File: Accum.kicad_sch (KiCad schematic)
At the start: 0 parts

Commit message: VER1.0: добавил схему в пдф
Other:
- note added: "Аналоговый сигнал"
- note added: "Арматура накопителя"
- note added: "Питание 24В"
- note added: "Управление 24В"
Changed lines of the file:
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@@
+	)
+	(rectangle
+		(start 146.05 88.9)
+		(end 490.22 325.12)
+		(stroke
+			(width 0.762)
+			(type dash)
+			(color 0 0 0 1)
+		)
+		(fill
+			(type none)
+		)
 	)
 	(rectangle
@@
 		)
 	)
+	(text "Питание 24В"
+		(exclude_from_sim no)
+		(at 73.66 361.95 0)
+		(effects
+			(font
+				(face "Calibri")
+				(size 2.54 2.54)
+				(thickness 0.254)
+				(bold yes)
+				(italic yes)
+				(color 0 0 0 1)
+			)
+			(justify left)
+		)
+	)
+	(text "Аналоговый сигнал"
+		(exclude_from_sim no)
+		(at 73.66 351.79 0)
+		(effects
+			(font
+				(face "Calibri")
+				(size 2.54 2.54)
+				(thickness 0.254)
+				(bold yes)
+				(italic yes)
+				(color 0 0 0 1)
+			)
+			(justify left)
+		)
+	)
 	(text "Р"
 		(exclude_from_sim no)
@@
 		)
 	)
+	(text "Управление 24В"
+		(exclude_from_sim no)
+		(at 73.66 367.03 0)
+		(effects
+			(font
+				(face "Calibri")
+				(size 2.54 2.54)
+				(thickness 0.254)
+				(bold yes)
+				(italic yes)
+				(color 0 0 0 1)
+			)
+			(justify left)
+		)
+	)
+	(text "Арматура накопителя"
+		(exclude_from_sim no)
+		(at 313.944 109.22 0)
+		(effects
+			(font
+				(face "Calibri")
+				(size 6.35 6.35)
+				(italic yes)
+				(color 0 0 0 1)
+			)
+		)
+	)
 	(text "+24В"
 		(exclude_from_sim no)
@@
 				(color 0 0 0 1)
 			)
+		)
+	)
+	(text "CAN сеть"
+		(exclude_from_sim no)
+		(at 73.66 356.87 0)
+		(effects
+			(font
+				(face "Calibri")
+				(size 2.54 2.54)
+				(thickness 0.254)
+				(bold yes)
+				(italic yes)
+				(color 0 0 0 1)
+			)
+			(justify left)
 		)
 	)
@@
 			(width 0.762)
 			(type solid)
+			(color 72 72 72 1)
 		)
 	)
@@
 			(width 0.762)
 			(type solid)
+			(color 72 72 72 1)
 		)
 	)
@@
 			(width 0.762)
 			(type solid)
+			(color 72 72 72 1)
 		)
 	)
@@
 			(width 0.762)
 			(type solid)
+			(color 72 72 72 1)
 		)
 	)
@@
 			(width 0.762)
 			(type solid)
+			(color 72 72 72 1)
 		)
 	)
@@
 			(width 0.762)
 			(type solid)
+			(color 72 72 72 1)
 		)
 	)
@@
 			(width 0.762)
 			(type solid)
+			(color 72 72 72 1)
 		)
 	)
@@
 			(width 0.762)
 			(type solid)
+			(color 72 72 72 1)
+		)
+	)
+	(polyline
+		(pts
+			(xy 55.88 356.87) (xy 71.12 356.87)
+		)
+		(stroke
+			(width 1.27)
+			(type solid)
+			(color 0 194 0 1)
+		)
+	)
+	(polyline
+		(pts
+			(xy 55.88 361.95) (xy 71.12 361.95)
+		)
+		(stroke
+			(width 1.27)
+			(type solid)
+			(color 194 0 0 1)
+		)
+	)
+	(polyline
+		(pts
+			(xy 55.88 367.03) (xy 71.12 367.03)
+		)
+		(stroke
+			(width 1.27)
+			(type solid)
+			(color 0 0 255 1)
 		)
 	)
@@
 			(width 0.762)
 			(type solid)
+			(color 72 72 72 1)
 		)
 	)
@@
 			(width 0.762)
 			(type solid)
+			(color 72 72 72 1)
 		)
 	)
@@
 	(polyline
 		(pts
-			(xy 332.74 166.37) (xy 396.24 166.37)
+			(xy 332.74 166.37) (xy 497.84 166.37)
 		)
 		(stroke
@@
 			(width 0.762)
 			(type solid)
+			(color 72 72 72 1)
 		)
 	)
@@
 			(width 0.762)
 			(type solid)
+			(color 72 72 72 1)
 		)
 	)
@@
 	(polyline
 		(pts
-			(xy 332.74 182.88) (xy 396.24 182.88)
+			(xy 332.74 182.88) (xy 497.84 182.88)
 		)
 		(stroke
@@
 			(width 0.762)
 			(type solid)
+			(color 72 72 72 1)
 		)
 	)
@@
 			(width 0.762)
 			(type solid)
+			(color 72 72 72 1)
 		)
 	)
@@
 			(width 0.762)
 			(type solid)
+			(color 72 72 72 1)
 		)
 	)
@@
 			(width 0.762)
 			(type solid)
-		)
-	)
+			(color 72 72 72 1)
+		)
+	)
+	(polyline
+		(pts
+			(xy 55.88 351.79) (xy 71.12 351.79)
+		)
+		(stroke
+			(width 1.27)
+			(type solid)
+			(color 72 72 72 1)
+		)
+	)

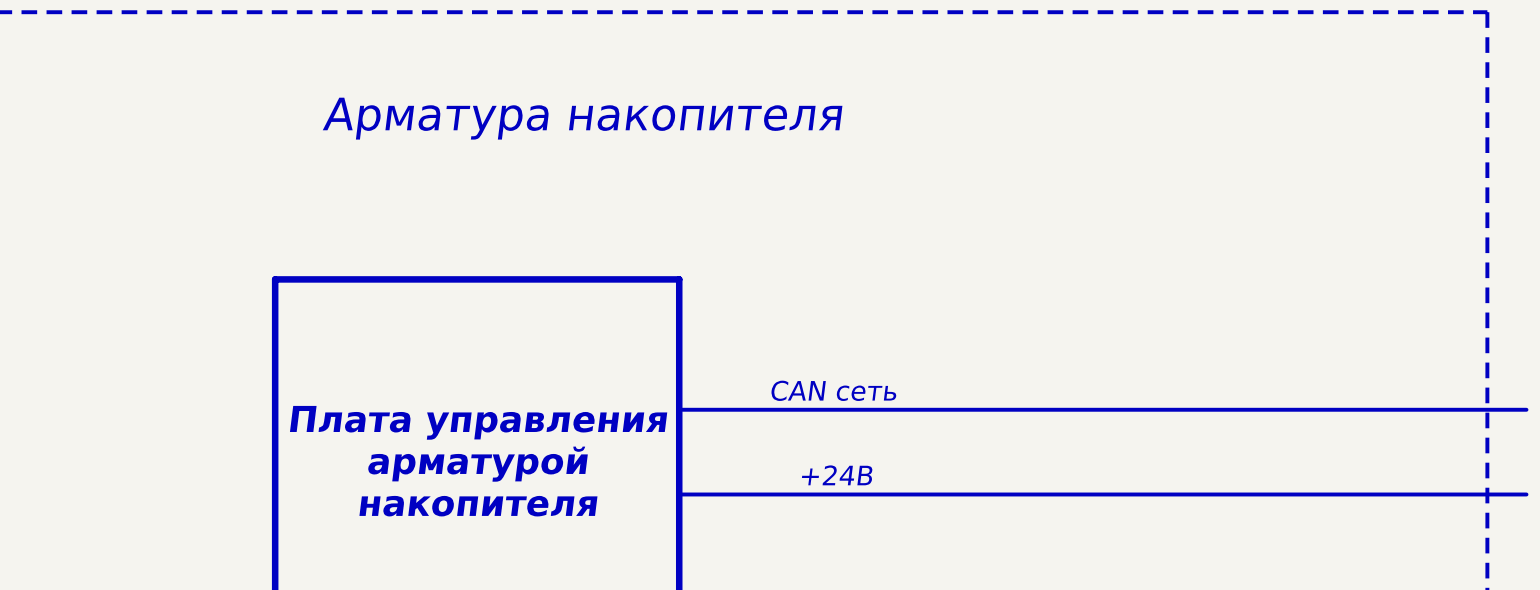
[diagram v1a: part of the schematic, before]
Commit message: VER1.0: исправил часть замечаний по схеме
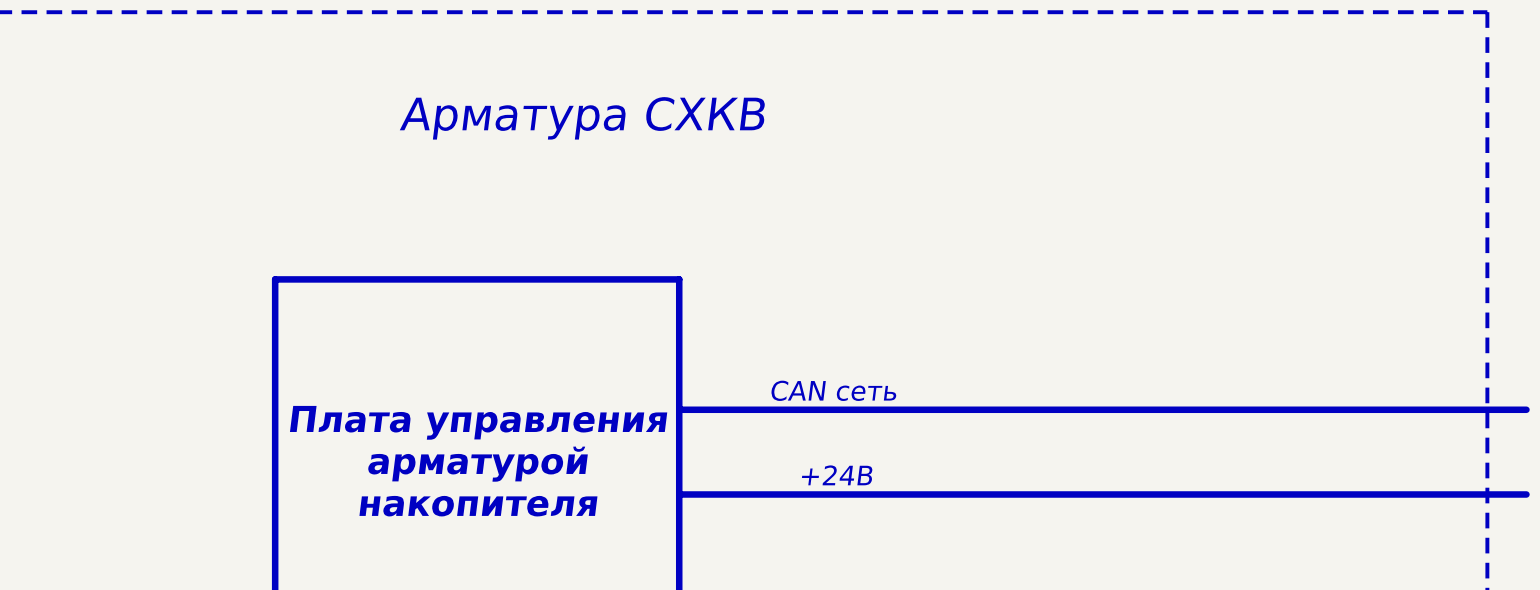
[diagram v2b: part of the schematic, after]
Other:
- note added: "Арматура СХКВ"
- note removed: "Арматура накопителя"
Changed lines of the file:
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@@
 		)
 	)
-	(text "Арматура накопителя"
+	(text "Арматура СХКВ"
 		(exclude_from_sim no)
 		(at 313.944 109.22 0)
@@
 		)
 		(stroke
-			(width 0.762)
+			(width 1.27)
 			(type solid)
 			(color 0 194 0 1)
@@
 		)
 		(stroke
-			(width 0.762)
+			(width 1.27)
 			(type solid)
 			(color 194 0 0 1)

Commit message: refactor for new ver
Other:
- note added: "CAN сеть (КИС-В)"
- note added: "Аналоговый сигнал (Например, МКЭШ 1,5)"
- note added: "Безопасная зона"
- note added: "Питание 24В 2 x 1,5кв.мм (например, ПВС)"
- note added: "Управление 24В 2 х 1,5 кв.мм (например МКЭШ 1,5)"
- note removed: "Аналоговый сигнал"
- note removed: "Питание 24В"
- note removed: "Управление 24В"

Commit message: version for piter
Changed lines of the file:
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@@
 	)
 	(rectangle
-		(start 396.24 88.9)
+		(start 384.81 88.9)
 		(end 490.22 325.12)
 		(stroke
